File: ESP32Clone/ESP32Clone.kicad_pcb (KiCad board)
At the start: 2 copper layers, 54 parts, among them J1 Connector, USB-TYPE-C-16P, J2 Conn_01x08_Pin, J3 Conn_01x08_Pin, U1 TPS54331DR, U2 ESP32-C3FH4, U3 AHT20, U4 BH1750FVI-TR, U5 24LC1025-I_SM, X1 40MHz, 15pF

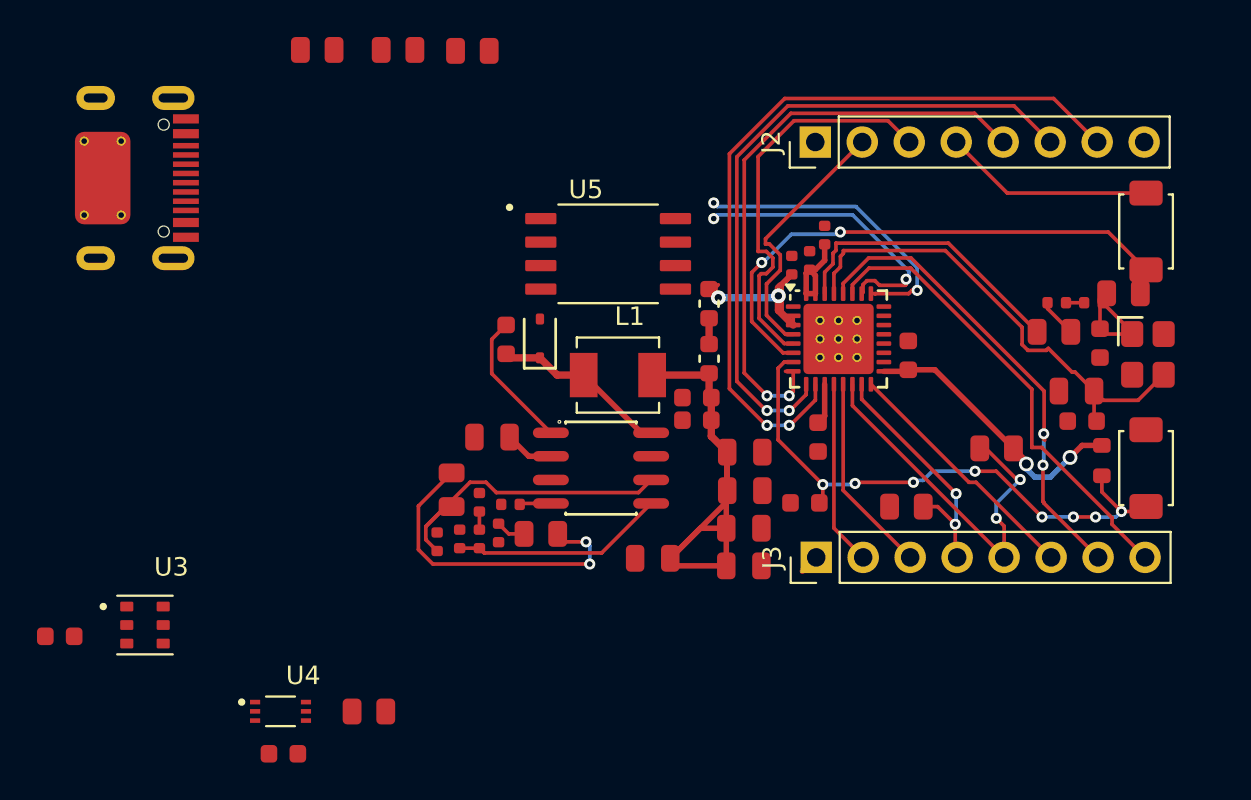
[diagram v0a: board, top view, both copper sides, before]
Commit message: Done DRC
only has a few library issue's left
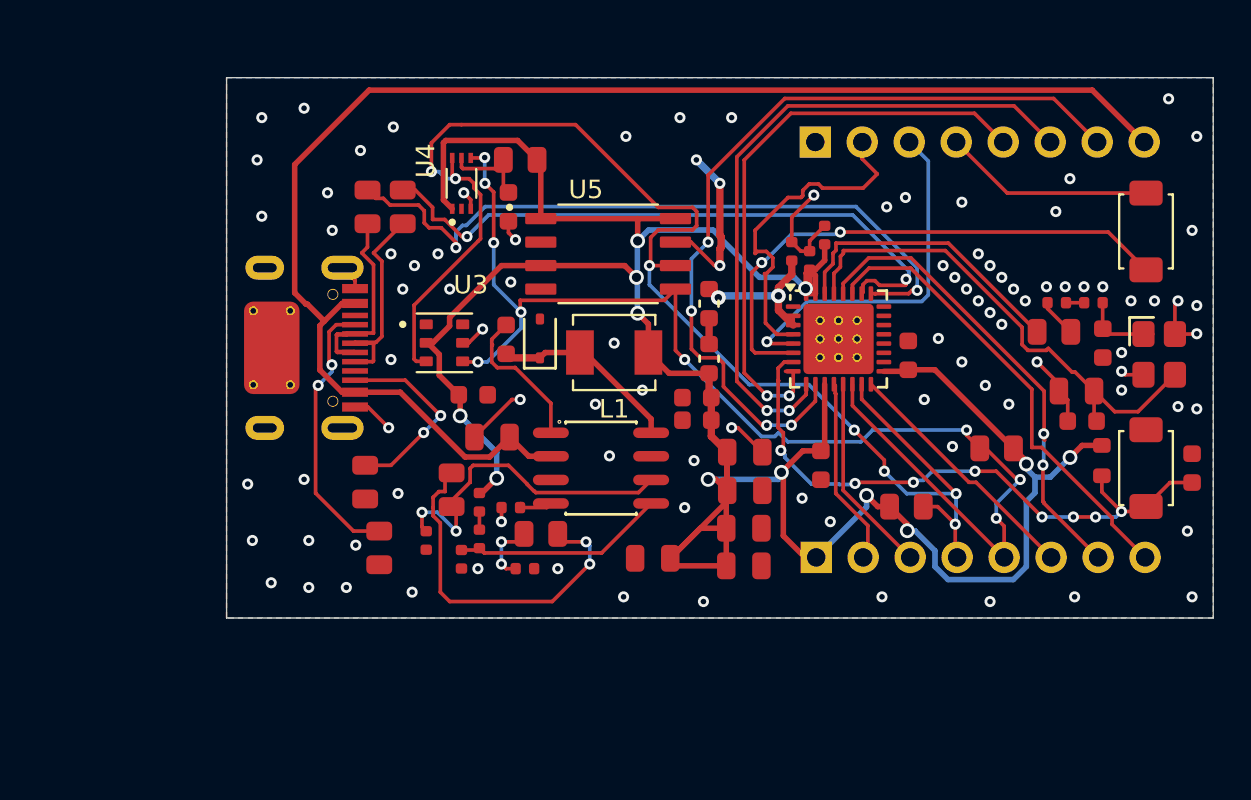
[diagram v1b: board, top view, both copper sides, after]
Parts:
- J2, J3: moved to B.Cu
- moved R7 42.2 mm to (83.1, 36.5), turned to -90 degrees
- moved C18 32.0 mm to (90.8, 21.6), turned to 90 degrees
- moved R15 30.9 mm to (91.4, 19.1)
- moved U4 30.2 mm to (88.3, 20.3), turned to 90 degrees
- moved R6 27.3 mm to (83.8, 40.0), turned to -90 degrees
- moved C17 25.9 mm to (88.9, 31.8)
- moved U3 22.2 mm to (87.3, 28.9)
- moved C16 21.0 mm to (127.8, 35.7), turned to 90 degrees
- moved J1 13.0 mm to (80.0, 29.2)
- moved R12 9.66 mm to (85.1, 21.6), turned to 90 degrees
- moved R11 8.64 mm to (83.2, 21.6), turned to 90 degrees
- moved C3 2.40 mm to (91.7, 41.1), turned to 180 degrees
- moved C7 1.53 mm to (107.7, 35.6)
- moved L1 1.24 mm to (96.5, 29.5)
- moved R2 1.10 mm to (88.3, 40.6), turned to -90 degrees
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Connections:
- net Net-(U2-GPIO18/USB_D-) renamed /USB D-
- net Net-(U2-GPIO19/USB_D+) renamed /USB D+
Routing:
- net /3.3V: track 51.6 -> 152.2 mm, vias 2 -> 12
- net /5V: track 2.66 -> 78.0 mm
- net /SCL: track 13.7 -> 76.6 mm, vias 2 -> 7
- net /SDA: track 20.6 -> 67.4 mm, vias 2 -> 9
- net GND: track 0.00 -> 36.9 mm, vias 0 -> 96
- net /USB D-: track 16.2 -> 38.1 mm
- net /USB D+: track 15.7 -> 34.4 mm
- net Net-(J1-CC1): track 0.00 -> 15.0 mm, vias 0 -> 2
- net /USB-C D-: track 0.00 -> 12.4 mm
- net /USB-C D+: track 0.00 -> 11.5 mm
- net Net-(J1-CC2): track 0.00 -> 11.1 mm, vias 0 -> 2
- net Net-(U4-DVI): track 0.00 -> 4.87 mm
- net /GPIO 0: track 14.2 -> 18.2 mm
- net /GPIO 5: track 41.7 -> 44.1 mm, vias 2 -> 4
- net /CHIP_EN: track 30.7 -> 33.1 mm
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- added copper zone on B.Cu, net GND
- added copper zone on F.Cu, net GND
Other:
- board outline added: 53.3 x 29.2 mm
- board text added: "V1"

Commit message: added silkscreen
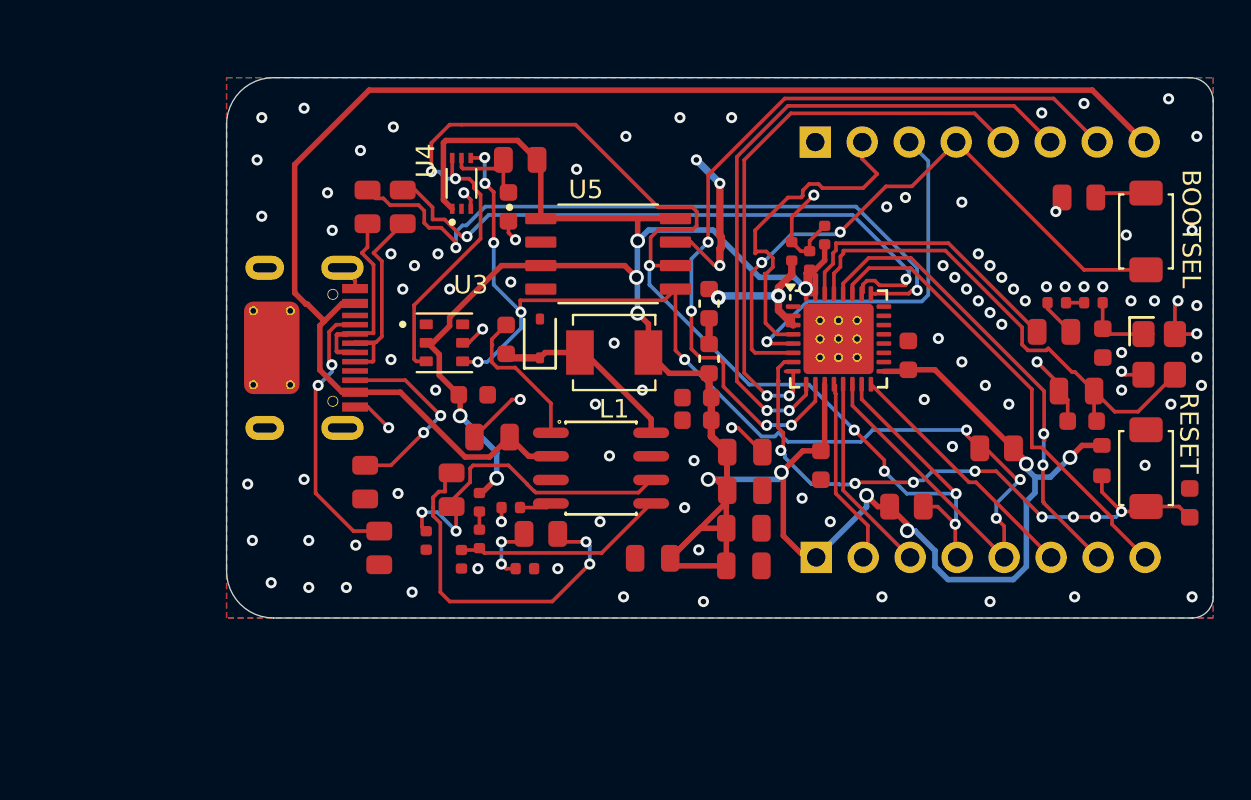
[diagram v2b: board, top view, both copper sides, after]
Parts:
- added R14: 150Ω, PCM_JLCPCB:R_0805, F.Cu at (121.6, 21.1)
- moved C16 1.88 mm to (127.6, 37.6)
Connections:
- S2 pad 1: /GPIO 2 -> Net-(S2-A)
- S2 pad 2: /GPIO 2/IN -> /GPIO 2
- U2 pad 6: /GPIO 2/IN -> /GPIO 2
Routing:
- net /GPIO 2/IN: track 29.5 -> 0.00 mm, vias 2 -> 0
- net /GPIO 2: track 11.4 -> 33.6 mm, vias 0 -> 2
- net Net-(S2-A): track 0.00 -> 2.82 mm
- net GND: vias 96 -> 103
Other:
- outline, holes or cut-outs redrawn
- board text added: "3.3V"
- board text added: "5V"
- board text added: "BOOTSEL"
- board text added: "ESP32 Clone with i2c sensors and eeprom"
- board text added: "GND"
- board text added: "IO 0"
- board text added: "IO 1"
- board text added: "IO 10"
- board text added: "IO 2"
- board text added: "IO 20"
- board text added: "IO 21"
- board text added: "IO 3"
- board text added: "IO 4"
- board text added: "IO 5"
- board text added: "IO 6"
- board text added: "IO 7"
- board text added: "Made by Adam Langeveld"
- board text added: "Made on <date>"
- board text added: "RESET"
- board text added: "SCL"
- board text added: "SDA"

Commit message: added funny koala
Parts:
- added G***: LOGO, Koala:koala, B.Cu at (90.6, 25.8)

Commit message: cleaned up files
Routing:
- net GND: vias 103 -> 104
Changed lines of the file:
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@@
 	)
 	(via
-		(at 86.868 31.496)
-		(size 0.6)
-		(drill 0.3)
-		(layers "F.Cu" "B.Cu")
-		(free yes)
-		(net 1)
-	)
-	(via
 		(at 95.504 32.258)
 		(size 0.6)
@@
 	)
 	(via
+		(at 109.855 35.306)
+		(size 0.6)
+		(drill 0.3)
+		(layers "F.Cu" "B.Cu")
+		(free yes)
+		(net 1)
+	)
+	(via
 		(at 123.952 31.496)
 		(size 0.6)
@@
 	)
 	(via
-		(at 128.27 31.242)
+		(at 127.9652 31.242)
 		(size 0.6)
 		(drill 0.3)
@@
 	)
 	(via
+		(at 105.029 23.114)
+		(size 0.6)
+		(drill 0.3)
+		(layers "F.Cu" "B.Cu")
+		(free yes)
+		(net 1)
+	)
+	(via
 		(at 85.725 24.765)
 		(size 0.6)
@@
 	)
 	(segment
-		(start 112.615 20.481)
-		(end 115.0112 18.0848)
+		(start 103.953 25.1436)
+		(end 103.953 29.293)
 		(width 0.2)
 		(layer "F.Cu")
@@
 	)
 	(segment
-		(start 103.953 25.1436)
-		(end 103.953 29.293)
+		(start 112.615 20.481)
+		(end 115.0112 18.0848)
 		(width 0.2)
 		(layer "F.Cu")
@@
 	)
 	(segment
-		(start 103.953 29.293)
-		(end 104.14 29.48)
+		(start 111.212935 20.481)
+		(end 112.615 20.481)
 		(width 0.2)
 		(layer "F.Cu")
@@
 	)
 	(segment
-		(start 108.742935 22.951)
+		(start 108.742934 22.951001)
 		(end 111.212935 20.481)
 		(width 0.2)
@@
 	)
 	(segment
-		(start 111.212935 20.481)
-		(end 112.615 20.481)
+		(start 108.680378 22.951001)
+		(end 108.742934 22.951001)
+		(width 0.2)
+		(layer "F.Cu")
+		(net 19)
+	)
+	(segment
+		(start 103.953 29.293)
+		(end 104.14 29.48)
 		(width 0.2)
 		(layer "F.Cu")
@@
 	)
 	(via
-		(at 108.742935 22.951)
+		(at 108.680378 22.951001)
 		(size 0.6)
 		(drill 0.3)
@@
 	)
 	(segment
-		(start 104.4966 24.6)
-		(end 104.570693 24.6)
+		(start 108.621842 23.072093)
+		(end 106.0986 23.072093)
 		(width 0.2)
 		(layer "B.Cu")
@@
 	)
 	(segment
-		(start 108.621842 23.072093)
-		(end 108.742935 22.951)
+		(start 108.680378 22.951001)
+		(end 108.680378 23.013557)
 		(width 0.2)
 		(layer "B.Cu")
@@
 	(segment
 		(start 104.570693 24.6)
-		(end 106.0986 23.072093)
+		(end 104.4966 24.6)
 		(width 0.2)
 		(layer "B.Cu")
@@
 	)
 	(segment
-		(start 106.0986 23.072093)
+		(start 108.680378 23.013557)
 		(end 108.621842 23.072093)
 		(width 0.2)
 		(layer "B.Cu")
+		(net 19)
+	)
+	(segment
+		(start 106.0986 23.072093)
+		(end 104.570693 24.6)
+		(width 0.2)
+		(layer "B.Cu")

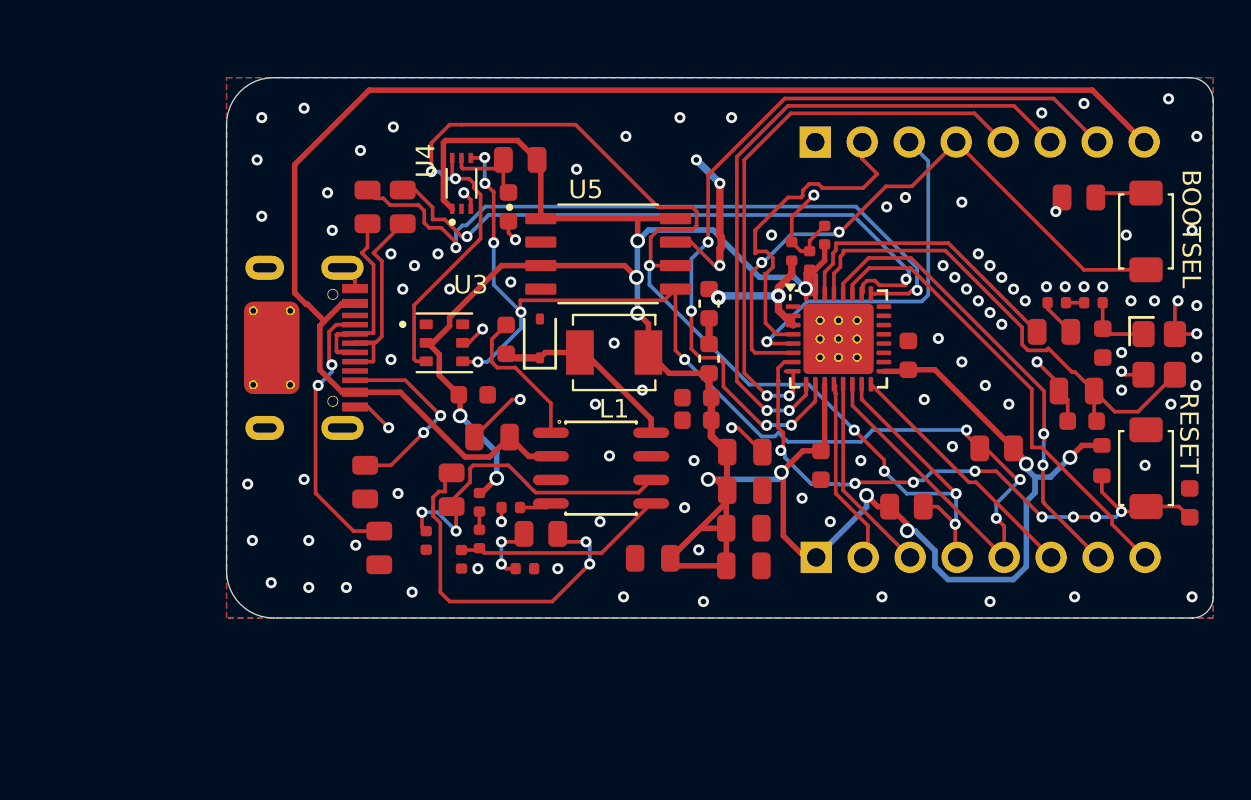
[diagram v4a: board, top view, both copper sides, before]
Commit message: Fixed DRC
DRC remianing:
3x Koala figure silkscreen clipped by something,
the koala is giant and doesnt give importent information so its fine
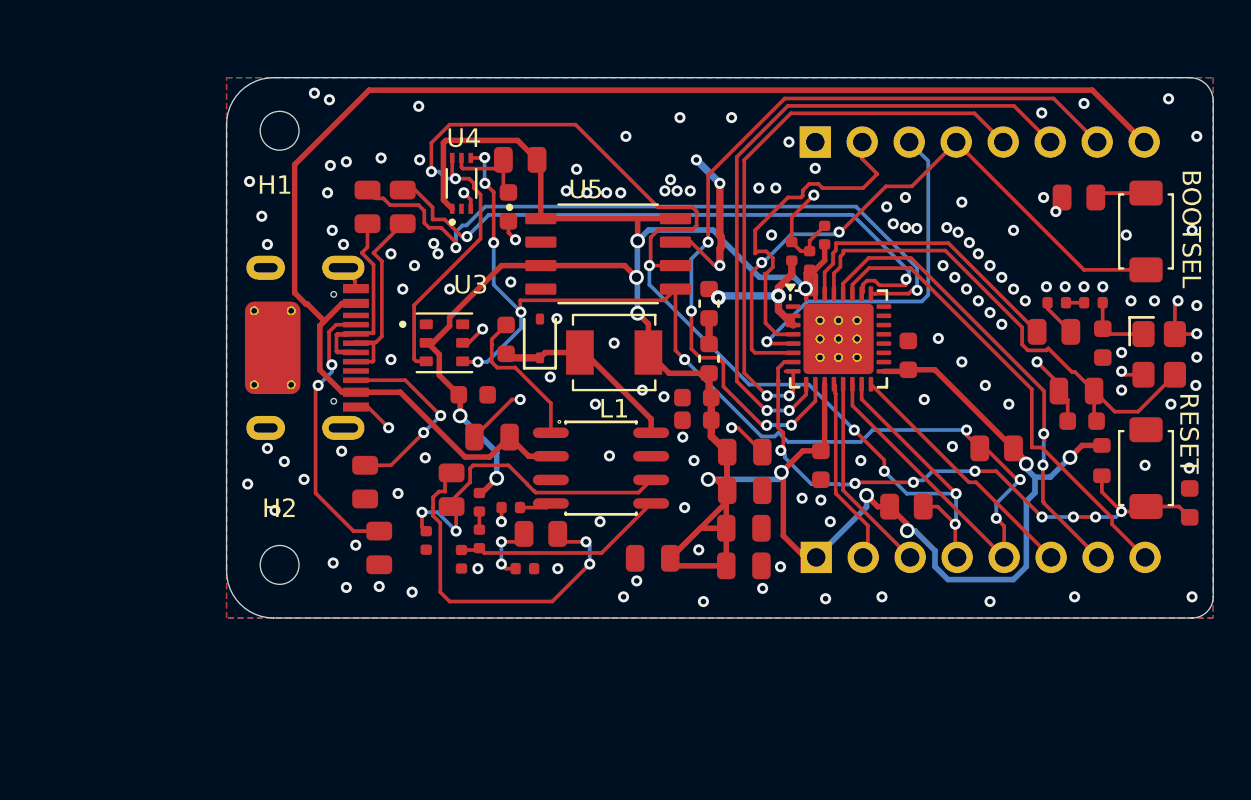
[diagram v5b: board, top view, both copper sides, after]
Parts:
- added H1: MountingHole, MountingHole:MountingHole_2.1mm, F.Cu at (78.4, 17.5)
- added H2: MountingHole, MountingHole:MountingHole_2.1mm, F.Cu at (78.4, 40.9)
- moved J1 0.05 mm to (80.1, 29.2)
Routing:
- net GND: vias 104 -> 143

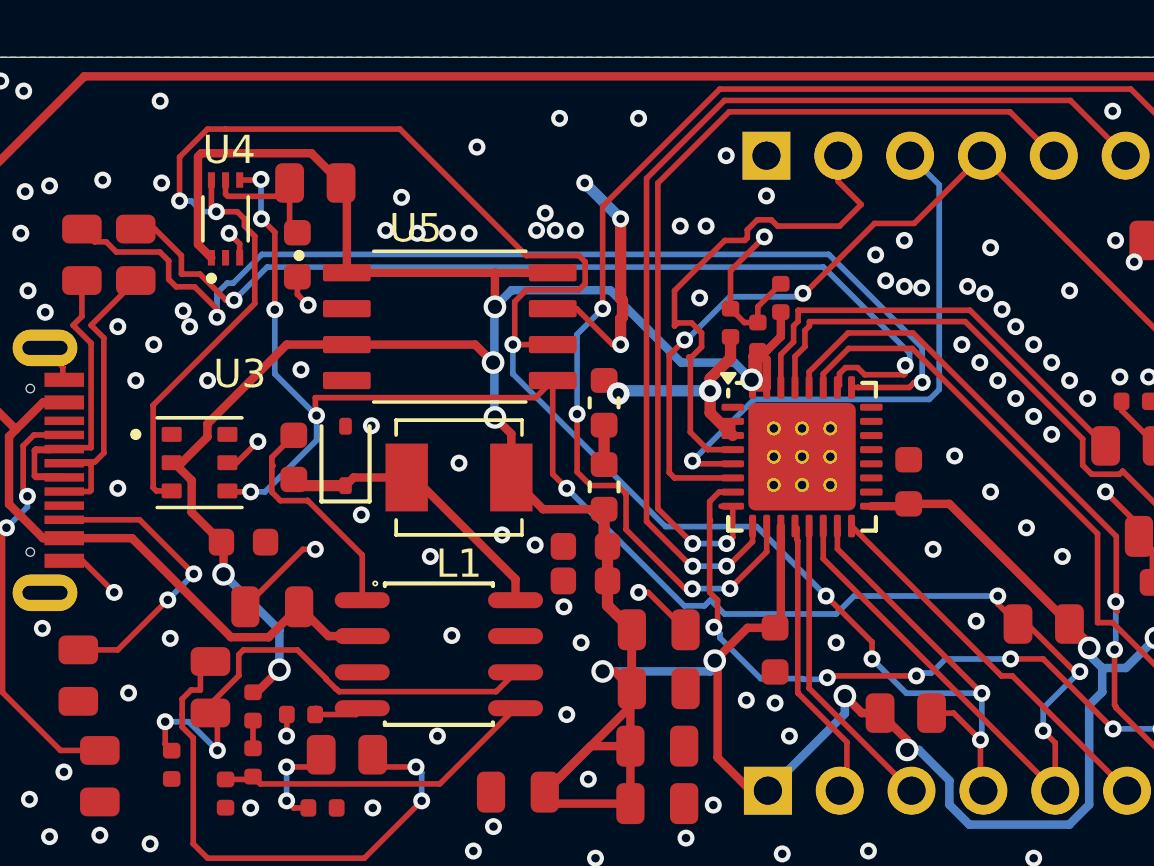
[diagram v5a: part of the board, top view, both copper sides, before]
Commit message: fixed long vsense wire
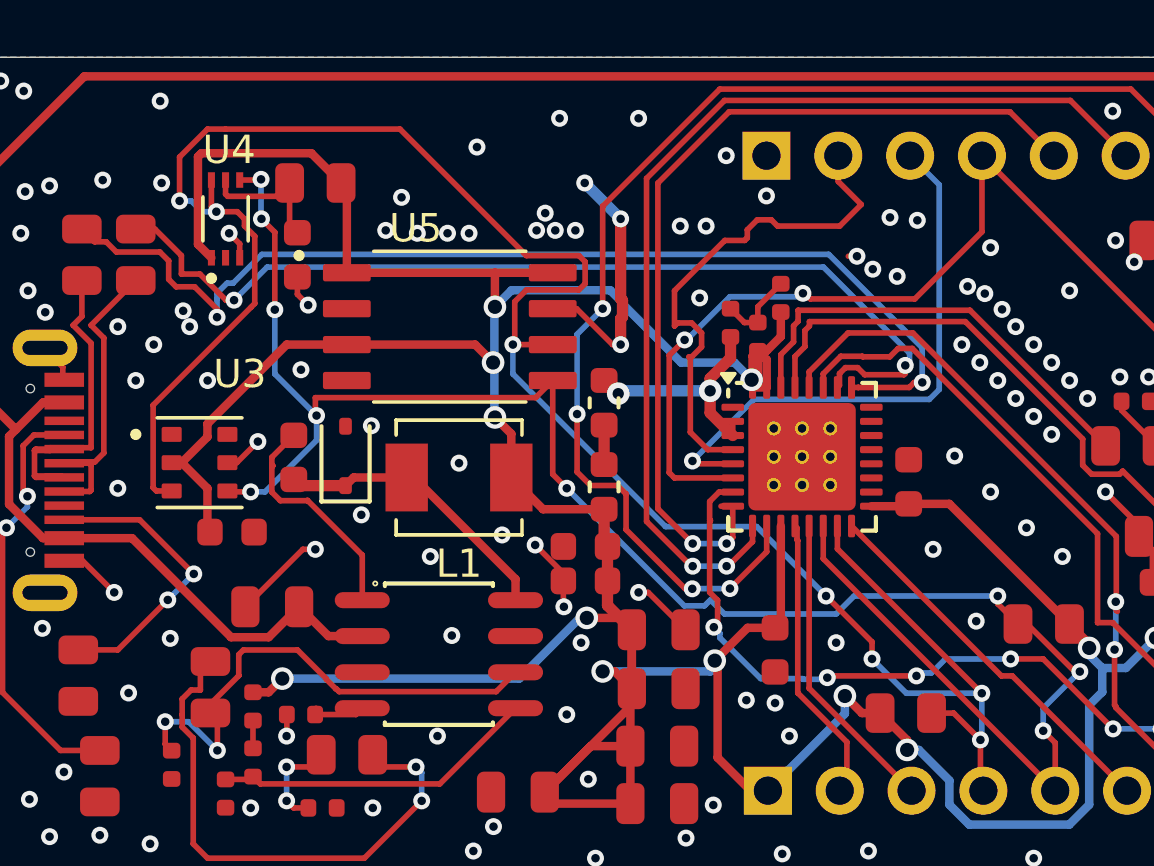
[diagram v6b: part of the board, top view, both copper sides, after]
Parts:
- moved C17 0.54 mm to (88.5, 31.4)
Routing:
- net /3.3V: track 152.2 -> 159.6 mm
- net /GPIO 2: track 33.6 -> 35.4 mm
- net GND: track 36.9 -> 36.8 mm, vias 143 -> 142
